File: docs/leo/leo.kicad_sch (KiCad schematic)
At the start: 17 parts, among them IC11 GAL16V8, IC20 74153, IC21 74LS273, IC29 74LS273, IC37 MB81C78A, IC40 74LS04, IC41 GAL16V8, IC51 GAL16V8, IC52 74LS32, IC56 74LS245, IC57 74LS245, IC61 74LS139, IC62 74LS20, IC8 7486

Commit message: Additional schematic updates
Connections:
- net ~{PALOBJ_WR}: now reaches IC41.17 (I03)
- net IC53_13 renamed IC63_13
- net IC53_158 renamed IC63_158
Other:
- added sheet Clock Generation (clock_gen.kicad_sch)
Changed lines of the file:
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@@
     )
   )
-  (global_label "IC53_158" (shape input) (at 157.48 110.49 180) (fields_autoplaced)
+  (global_label "IC63_158" (shape input) (at 157.48 110.49 180) (fields_autoplaced)
     (effects (font (size 1.27 1.27)) (justify right))
     (property "Intersheet References" "${INTERSHEET_REFS}" (id 0) (at 146.1769 110.4106 0)
@@
     )
   )
+  (global_label "~{PALOBJ_WR}" (shape input) (at 182.88 163.83 0) (fields_autoplaced)
+    (effects (font (size 1.27 1.27)) (justify left))
+    (property "Intersheet References" "${INTERSHEET_REFS}" (id 0) (at 195.9369 163.7506 0)
+      (effects (font (size 1.27 1.27)) (justify left) hide)
+    )
+  )
   (global_label "BUF_A17" (shape input) (at 157.48 171.45 180) (fields_autoplaced)
     (effects (font (size 1.27 1.27)) (justify right))
@@
     )
   )
-  (global_label "IC53_13" (shape input) (at 157.48 113.03 180) (fields_autoplaced)
+  (global_label "IC63_13" (shape input) (at 157.48 113.03 180) (fields_autoplaced)
     (effects (font (size 1.27 1.27)) (justify right))
     (property "Intersheet References" "${INTERSHEET_REFS}" (id 0) (at 147.3864 112.9506 0)
@@
   )
   (symbol (lib_id "power:GND") (at 1010.92 97.79 0) (unit 1)
-    (in_bom yes) (on_board yes) (fields_autoplaced)
+    (in_bom yes) (on_board yes)
     (property "Reference" "#PWR?" (id 0) (at 1010.92 104.14 0)
       (effects (font (size 1.27 1.27)) hide)
     )
-    (property "Value" "GND" (id 1) (at 1010.92 102.87 0))
+    (property "Value" "GND" (id 1) (at 1009.65 76.2 0)
+      (effects (font (size 1.27 1.27)) hide)
+    )
     (property "Footprint" "" (id 2) (at 1010.92 97.79 0)
       (effects (font (size 1.27 1.27)) hide)
@@
     )
   )
+  (sheet (at 130.81 41.91) (size 64.77 46.99) (fields_autoplaced)
+    (stroke (width 0.1524) (type solid) (color 0 0 0 0))
+    (fill (color 0 0 0 0.0000))
+    (property "Sheet name" "Clock Generation" (id 0) (at 130.81 41.1984 0)
+      (effects (font (size 1.27 1.27)) (justify left bottom))
+    )
+    (property "Sheet file" "clock_gen.kicad_sch" (id 1) (at 130.81 89.4846 0)
+      (effects (font (size 1.27 1.27)) (justify left top))
+    )
+  )
   (sheet_instances
     (path "/" (page "1"))
     (path "/3f170781-d744-477d-adf1-ed36cff99e11" (page "2"))
+    (path "/e1b825f4-123a-44fe-9974-9687a3e7c3da" (page "3"))
   )
   (symbol_instances
@@
       (reference "#PWR?") (unit 1) (value "GND") (footprint "")
     )
+    (path "/e1b825f4-123a-44fe-9974-9687a3e7c3da/bbdcfda0-3dba-4fe5-a36d-90bcbc474d51"
+      (reference "#PWR?") (unit 1) (value "VCC") (footprint "")
+    )
     (path "/3f170781-d744-477d-adf1-ed36cff99e11/c7de3329-b4e8-4d45-a030-6104281a2e4a"
       (reference "#PWR?") (unit 1) (value "VCC") (footprint "")
     )
+    (path "/e1b825f4-123a-44fe-9974-9687a3e7c3da/cddd6e94-3703-49bb-b5fb-1157ae64060d"
+      (reference "#PWR?") (unit 1) (value "GND") (footprint "")
+    )
     (path "/ce4df0e2-0cc3-4f87-abc0-3a5ec5d96545"
       (reference "#PWR?") (unit 1) (value "GND") (footprint "")
@@
       (reference "#PWR?") (unit 1) (value "VCC") (footprint "")
     )
+    (path "/e1b825f4-123a-44fe-9974-9687a3e7c3da/e00497ee-2791-45a8-a10c-616edd803b03"
+      (reference "#PWR?") (unit 1) (value "GND") (footprint "")
+    )
     (path "/e019aca8-6465-4011-810e-706da10ea3a1"
       (reference "#PWR?") (unit 1) (value "GND") (footprint "")
@@
       (reference "#PWR?") (unit 1) (value "GND") (footprint "")
     )
+    (path "/e1b825f4-123a-44fe-9974-9687a3e7c3da/f4ea3a91-454d-488f-8b67-734daec0d3cf"
+      (reference "#PWR?") (unit 1) (value "VCC") (footprint "")
+    )
+    (path "/e1b825f4-123a-44fe-9974-9687a3e7c3da/ac127c66-37c5-4e45-b9ed-1d368539500b"
+      (reference "C?") (unit 1) (value "100pf") (footprint "")
+    )
+    (path "/e1b825f4-123a-44fe-9974-9687a3e7c3da/dbe43588-c00f-498b-be57-e4350aabd804"
+      (reference "FL?") (unit 1) (value "Filter_EMI_LCL") (footprint "")
+    )
     (path "/28065ba0-9d76-40f7-b01f-ddcb5b52082b"
       (reference "IC8") (unit 3) (value "7486") (footprint "")
     )
+    (path "/3f170781-d744-477d-adf1-ed36cff99e11/395fec3c-8586-4f0e-bf07-2d42c6cd9977"
+      (reference "IC9") (unit 1) (value "74LS273") (footprint "")
+    )
+    (path "/3f170781-d744-477d-adf1-ed36cff99e11/4d3531a9-962e-4c63-9d05-3371072e72d3"
+      (reference "IC10") (unit 1) (value "74LS273") (footprint "")
+    )
     (path "/f3acd7cf-5b39-4952-ac2d-708abf87baf7"
       (reference "IC11") (unit 1) (value "GAL16V8") (footprint "")
@@
       (reference "IC21") (unit 1) (value "74LS273") (footprint "")
     )
+    (path "/3f170781-d744-477d-adf1-ed36cff99e11/396eddf3-6537-423f-9156-11f40f4239d7"
+      (reference "IC22") (unit 1) (value "74LS245") (footprint "")
+    )
+    (path "/3f170781-d744-477d-adf1-ed36cff99e11/67263d0f-a492-4d36-83e2-ce10774430c9"
+      (reference "IC23") (unit 1) (value "74LS245") (footprint "")
+    )
     (path "/3f170781-d744-477d-adf1-ed36cff99e11/f833f0c3-4fce-4dd4-96ab-bbcda0f1502d"
       (reference "IC25") (unit 1) (value "74153") (footprint "")
@@
       (reference "IC29") (unit 1) (value "74LS273") (footprint "")
     )
+    (path "/3f170781-d744-477d-adf1-ed36cff99e11/df1e08b2-8b8d-453d-ab0a-2d347b006dd1"
+      (reference "IC30") (unit 1) (value "74LS374") (footprint "")
+    )
+    (path "/3f170781-d744-477d-adf1-ed36cff99e11/3be7a7e4-dc43-4016-88a4-123bf7e89b22"
+      (reference "IC31") (unit 1) (value "74LS374") (footprint "")
+    )
     (path "/543537a5-77fb-40a8-8960-21af55848bb6"
       (reference "IC37") (unit 1) (value "MB81C78A") (footprint "Package_DIP:DIP-28_W15.24mm")
@@
       (reference "IC52") (unit 4) (value "74LS32") (footprint "")
     )
+    (path "/e1b825f4-123a-44fe-9974-9687a3e7c3da/ecb187f6-9f43-4a6d-a23e-63a8f8ee5440"
+      (reference "IC53") (unit 1) (value "74LS74") (footprint "")
+    )
+    (path "/e1b825f4-123a-44fe-9974-9687a3e7c3da/9fe5efa2-2163-4ec3-9e8a-f4c507871a11"
+      (reference "IC53") (unit 2) (value "74LS74") (footprint "")
+    )
+    (path "/e1b825f4-123a-44fe-9974-9687a3e7c3da/562b00a1-2226-40cb-b257-7c82441dcb45"
+      (reference "IC54") (unit 2) (value "7404") (footprint "")
+    )
     (path "/0a9fe7a0-5a11-4224-a0fd-9dd12299da07"
       (reference "IC56") (unit 1) (value "74LS245") (footprint "")
@@
       (reference "U?") (unit 3) (value "74LS139") (footprint "")
     )
-  )
+    (path "/e1b825f4-123a-44fe-9974-9687a3e7c3da/e4eef5b5-6eda-476f-860f-184fabb2fab7"
+      (reference "U?") (unit 3) (value "74LS74") (footprint "")
+    )
+    (path "/e1b825f4-123a-44fe-9974-9687a3e7c3da/b7ae7790-350f-4215-b7e9-eb024ebb4f40"
+      (reference "X2") (unit 1) (value "26.6666Mhz") (footprint "Oscillator:Oscillator_DIP-14")
+    )
+  )

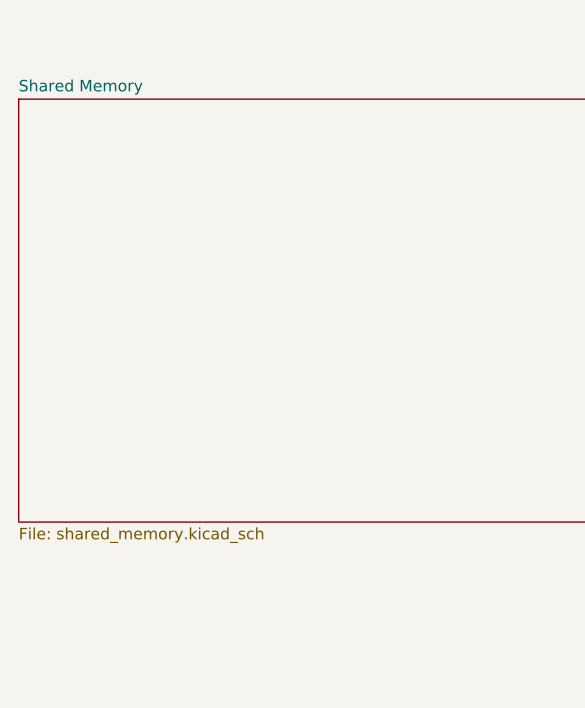
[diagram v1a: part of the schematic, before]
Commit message: Renamed shared ram
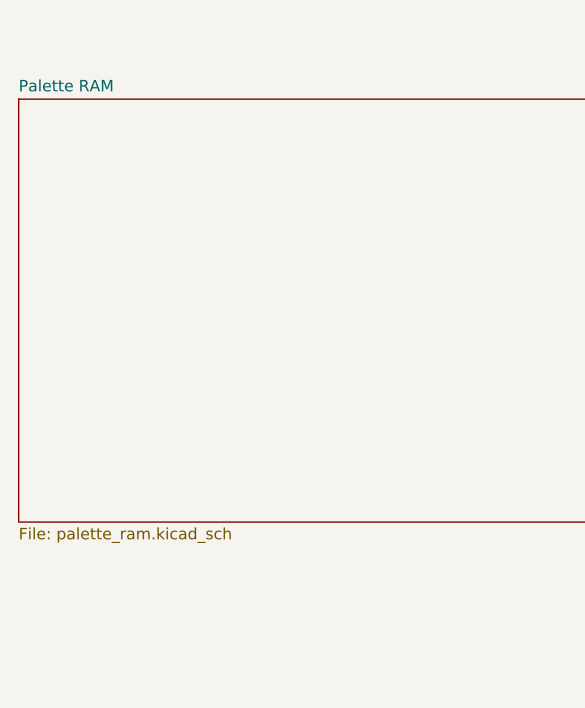
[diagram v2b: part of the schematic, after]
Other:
- sheet Shared Memory renamed Palette RAM
- sheet Palette RAM: file shared_memory.kicad_sch -> palette_ram.kicad_sch
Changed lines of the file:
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@@
     (stroke (width 0.1524) (type solid) (color 0 0 0 0))
     (fill (color 0 0 0 0.0000))
-    (property "Sheet name" "Shared Memory" (id 0) (at 55.88 41.1984 0)
+    (property "Sheet name" "Palette RAM" (id 0) (at 55.88 41.1984 0)
       (effects (font (size 1.27 1.27)) (justify left bottom))
     )
-    (property "Sheet file" "shared_memory.kicad_sch" (id 1) (at 55.88 89.4846 0)
+    (property "Sheet file" "palette_ram.kicad_sch" (id 1) (at 55.88 89.4846 0)
       (effects (font (size 1.27 1.27)) (justify left top))
     )

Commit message: schematic updates
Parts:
- added IC38: MB81C78A, Package_DIP:DIP-28_W15.24mm, symbol Irem:MB81C78A
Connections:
- net BUF_D0 is gone; now on net CPU_D0: IC21.8 (D3), IC56.9 (A7), RA18.2 (R1)
- net BUF_D1 is gone; now on net CPU_D1: IC21.13 (D4), IC56.8 (A6), RA18.3 (R2)
- net BUF_D10 is gone; now on net CPU_D10: IC29.7 (D2), IC57.7 (A5), RA19.4 (R3)
- net BUF_D11 is gone; now on net CPU_D11: IC29.14 (D5), IC57.6 (A4), RA19.5 (R4)
- net BUF_D12 is gone; now on net CPU_D12: IC29.4 (D1), IC57.5 (A3), RA19.6 (R5)
- net BUF_D13 is gone; now on net CPU_D13: IC29.17 (D6), IC57.4 (A2), RA19.7 (R6)
- net BUF_D14 is gone; now on net CPU_D14: IC29.3 (D0), IC57.3 (A1), RA19.8 (R7)
- net BUF_D15 is gone; now on net CPU_D15: IC29.18 (D7), IC57.2 (A0), RA19.9 (R8)
- net BUF_D2 is gone; now on net CPU_D2: IC21.7 (D2), IC56.7 (A5), RA18.4 (R3)
- net BUF_D3 is gone; now on net CPU_D3: IC21.14 (D5), IC56.6 (A4), RA18.5 (R4)
- net BUF_D4 is gone; now on net CPU_D4: IC21.4 (D1), IC56.5 (A3), RA18.6 (R5)
- net BUF_D5 is gone; now on net CPU_D5: IC21.17 (D6), IC56.4 (A2), RA18.7 (R6)
- net BUF_D6 is gone; now on net CPU_D6: IC21.3 (D0), IC56.3 (A1), RA18.8 (R7)
- net BUF_D7 is gone; now on net CPU_D7: IC21.18 (D7), IC56.2 (A0), RA18.9 (R8)
- net BUF_D8 is gone; now on net CPU_D8: IC29.8 (D3), IC57.9 (A7), RA19.2 (R1)
- net BUF_D9 is gone; now on net CPU_D9: IC29.13 (D4), IC57.8 (A6), RA19.3 (R2)
- net CPU_D0: no longer IC56.11 (B7)
- net CPU_D1: no longer IC56.12 (B6)
- net CPU_D10: no longer IC57.13 (B5)
- net CPU_D11: no longer IC57.14 (B4)
- net CPU_D12: no longer IC57.15 (B3)
- net CPU_D13: no longer IC57.16 (B2)
- net CPU_D14: no longer IC57.17 (B1)
- net CPU_D15: no longer IC57.18 (B0)
- net CPU_D2: no longer IC56.13 (B5)
- net CPU_D3: no longer IC56.14 (B4)
- net CPU_D4: no longer IC56.15 (B3)
- net CPU_D5: no longer IC56.16 (B2)
- net CPU_D6: no longer IC56.17 (B1)
- net CPU_D7: no longer IC56.18 (B0)
- net CPU_D8: no longer IC57.11 (B7)
- net CPU_D9: no longer IC57.12 (B6)
- net GND: now also IC37.14 (GND), IC38.14 (GND), IC38.22 (~{OE})
- net VCC: now also IC37.26 (CS2), IC37.28 (VCC), IC38.26 (CS2), IC38.28 (VCC)
- net BUFFER_D0: now reaches IC37.11 (IO1)
- net BUFFER_D1: now reaches IC37.12 (IO2)
- net BUFFER_D2: now reaches IC37.13 (IO3)
- net BUFFER_D3: now reaches IC37.15 (IO4)
- net BUFFER_D4: now reaches IC37.16 (IO5)
- net BUFFER_D5: now reaches IC37.17 (IO6)
- net BUFFER_D6: now reaches IC37.18 (IO7)
- net BUFFER_D7: now reaches IC37.19 (IO8)
- net LINE2_A0 renamed BUFFERB_A0
- net BUFFERB_A0: now also IC38.23 (A0)
- net LINE2_A3 renamed BUFFERB_A3
- net BUFFERB_A3: now also IC38.21 (A3)
- net LINE2_A4 renamed BUFFERB_A4
- net BUFFERB_A4: now also IC38.2 (A4)
- net LINE_A1 renamed BUFFER_A1
- net BUFFER_A1: now also IC38.24 (A1)
- net LINE_A10 renamed BUFFER_A10
- net BUFFER_A10: now also IC38.8 (A10)
- net LINE_A11 renamed BUFFER_A11
- net BUFFER_A11: now also IC38.9 (A11)
- net LINE_A12 renamed BUFFER_A12
- net BUFFER_A12: now also IC38.10 (A12)
- net LINE_A2 renamed BUFFER_A2
- net BUFFER_A2: now also IC38.25 (A2)
- net LINE_A4 renamed BUFFER_A4
- net LINE_A5 renamed BUFFER_A5
- net BUFFER_A5: now also IC38.3 (A5)
- net LINE_A6 renamed BUFFER_A6
- net BUFFER_A6: now also IC38.4 (A6)
- net LINE_A7 renamed BUFFER_A7
- net BUFFER_A7: now also IC38.5 (A7)
- net LINE_A8 renamed BUFFER_A8
- net BUFFER_A8: now also IC38.6 (A8)
- net LINE_A9 renamed BUFFER_A9
- net BUFFER_A9: now also IC38.7 (A9)
- net ~{CPU_DSTB} renamed ~{V33_DSTB}
- net ~{LINE_CS} renamed ~{BUFFER_CS}
- net ~{BUFFER_CS}: now also IC38.20 (~{CS1})
- net ~{LINE_WE} renamed ~{BUFFER_WE}
- net ~{BUFFER_WE}: now also IC38.27 (~{WE})
- new net BUFFER_D10: IC38.13 (IO3)
- new net BUFFER_D11: IC38.15 (IO4)
- new net BUFFER_D12: IC38.16 (IO5)
- new net BUFFER_D13: IC38.17 (IO6)
- new net BUFFER_D14: IC38.18 (IO7)
- new net BUFFER_D15: IC38.19 (IO8)
- new net BUFFER_D8: IC38.11 (IO1)
- new net BUFFER_D9: IC38.12 (IO2)
- new net V33_D0: IC56.11 (B7)
- new net V33_D1: IC56.12 (B6)
- new net V33_D10: IC57.13 (B5)
- new net V33_D11: IC57.14 (B4)
- new net V33_D12: IC57.15 (B3)
- new net V33_D13: IC57.16 (B2)
- new net V33_D14: IC57.17 (B1)
- new net V33_D15: IC57.18 (B0)
- new net V33_D2: IC56.13 (B5)
- new net V33_D3: IC56.14 (B4)
- new net V33_D4: IC56.15 (B3)
- new net V33_D5: IC56.16 (B2)
- new net V33_D6: IC56.17 (B1)
- new net V33_D7: IC56.18 (B0)
- new net V33_D8: IC57.11 (B7)
- new net V33_D9: IC57.12 (B6)
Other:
- moved on the sheet: IC37

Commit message: Fixed up label names Added connectors sheet
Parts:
- added IC58, IC59, IC60: 74LS244, symbol 74xx:74LS244
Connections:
- net BUF_A17 is gone; now on net CPU_A17: IC41.6 (I6)
- net BUF_A18 is gone; now on net CPU_A18: IC41.5 (I5)
- net BUF_A19 is gone; now on net CPU_A19: IC41.4 (I4)
- net CPU_BUF_A16 is gone; now on net CPU_A16: IC52.2
- net GND: now also IC21.10 (GND), IC29.10 (GND), IC58.1 (OEa), IC58.10 (GND), IC58.19 (OEb), IC58.2 (I0a), IC59.1 (OEa), IC59.10 (GND), IC59.19 (OEb), IC60.1 (OEa), IC60.10 (GND), IC60.19 (OEb)
- net VCC: now also IC21.20 (VCC), IC29.20 (VCC), IC58.20 (VCC), IC59.20 (VCC), IC60.20 (VCC)
- net CPU_M/~{IO}: now reaches IC62.1
- net CPU_M/~{IO}: now also IC58.12 (O3a)
- net CPU_A19: now reaches IC62.2
- net CPU_A19: now also IC58.9 (O0b)
- net CPU_A18: now reaches IC62.4
- net CPU_A18: now also IC58.7 (O1b)
- net CPU_A17: now reaches IC62.5
- net CPU_A17: now also IC58.5 (O2b)
- net BUF_A1 renamed CPU_A1
- net CPU_A1: now also IC60.5 (O2b)
- net BUF_A11 renamed CPU_A11
- net CPU_A11: now also IC59.9 (O0b)
- net BUF_A12 renamed CPU_A12
- net CPU_A12: now also IC59.18 (O0a)
- net BUF_A13 renamed CPU_A13
- net CPU_A13: now also IC59.16 (O1a)
- net BUF_A14 renamed CPU_A14
- net CPU_A14: now also IC59.14 (O2a)
- net BUF_A15 renamed CPU_A15
- net CPU_A15: now also IC59.12 (O3a)
- net BUF_A16 renamed CPU_A16
- net CPU_A16: now also IC58.3 (O3b)
- net BUF_A5 renamed CPU_A5
- net CPU_A5: now also IC60.16 (O1a)
- net BUF_A6 renamed CPU_A6
- net CPU_A6: now also IC60.14 (O2a)
- net BUF_A7 renamed CPU_A7
- net CPU_A7: now also IC60.12 (O3a)
- net BUF_EN renamed ~{LS245_EN}
- net CPU_R~{W} renamed CPU_R/~{W}
- net CPU_R/~{W}: now also IC58.14 (O2a)
- new net CPU_A0: IC60.3 (O3b)
- new net CPU_A10: IC59.7 (O1b)
- new net CPU_A2: IC60.7 (O1b)
- new net CPU_A3: IC60.9 (O0b)
- new net CPU_A4: IC60.18 (O0a)
- new net CPU_A8: IC59.3 (O3b)
- new net CPU_A9: IC59.5 (O2b)
- new net CPU_UBE: IC58.16 (O1a)
- new net V33_A0: IC60.17 (I3b)
- new net V33_A1: IC60.15 (I2b)
- new net V33_A10: IC59.13 (I1b)
- new net V33_A11: IC59.11 (I0b)
- new net V33_A12: IC59.2 (I0a)
- new net V33_A13: IC59.4 (I1a)
- new net V33_A14: IC59.6 (I2a)
- new net V33_A15: IC59.8 (I3a)
- new net V33_A16: IC58.17 (I3b)
- new net V33_A17: IC58.15 (I2b)
- new net V33_A18: IC58.13 (I1b)
- new net V33_A19: IC58.11 (I0b)
- new net V33_A2: IC60.13 (I1b)
- new net V33_A3: IC60.11 (I0b)
- new net V33_A4: IC60.2 (I0a)
- new net V33_A5: IC60.4 (I1a)
- new net V33_A6: IC60.6 (I2a)
- new net V33_A7: IC60.8 (I3a)
- new net V33_A8: IC59.17 (I3b)
- new net V33_A9: IC59.15 (I2b)
- new net V33_M/~{IO}: IC58.8 (I3a)
- new net V33_R/~{W}: IC58.6 (I2a)
- new net V33_UBE: IC58.4 (I1a)
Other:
- added sheet Connectors (connectors.kicad_sch)
- moved on the sheet: IC29, IC52C, IC52D

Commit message: Added GA21 sheet
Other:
- added sheet GA 21 (ga_21.kicad_sch)
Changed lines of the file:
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@@
     (pin "9")
+  )
+  (sheet (at 285.75 41.91) (size 68.58 45.72) (fields_autoplaced)
+    (stroke (width 0.1524) (type solid) (color 0 0 0 0))
+    (fill (color 0 0 0 0.0000))
+    (property "Sheet name" "GA 21" (id 0) (at 285.75 41.1984 0)
+      (effects (font (size 1.27 1.27)) (justify left bottom))
+    )
+    (property "Sheet file" "ga_21.kicad_sch" (id 1) (at 285.75 88.2146 0)
+      (effects (font (size 1.27 1.27)) (justify left top))
+    )
   )
   (sheet (at 205.74 41.91) (size 68.58 46.99) (fields_autoplaced)
@@
     (path "/e1b825f4-123a-44fe-9974-9687a3e7c3da" (page "3"))
     (path "/3c8e9905-8b74-4eb3-9c18-3105ee09a33f" (page "4"))
+    (path "/0bd61519-701e-4675-a889-b424ac477c32" (page "5"))
   )
   (symbol_instances
@@
       (reference "IC41") (unit 1) (value "GAL16V8") (footprint "")
     )
+    (path "/0bd61519-701e-4675-a889-b424ac477c32/96db101b-ae4d-43b3-916e-917ab5e9ffef"
+      (reference "IC42") (unit 1) (value "GA21") (footprint "")
+    )
     (path "/433b0e72-de3e-455f-a050-17638acf1723"
